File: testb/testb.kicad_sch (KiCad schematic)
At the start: 3 parts

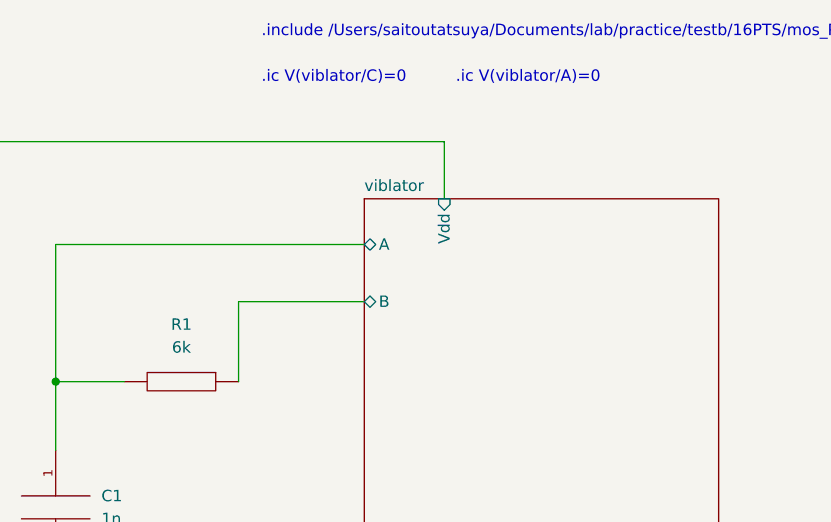
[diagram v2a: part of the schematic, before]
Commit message: マルチフィンガーにせず設計
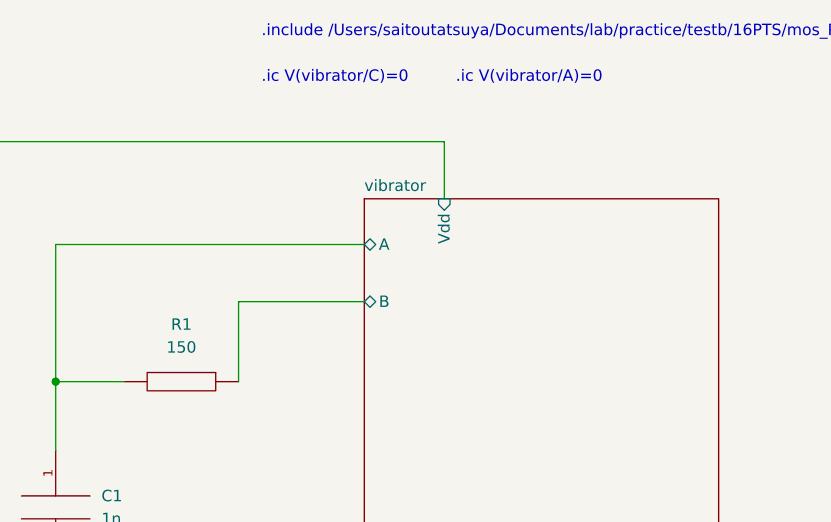
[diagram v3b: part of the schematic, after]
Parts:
- R1: value 6k -> 150
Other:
- sheet viblator renamed vibrator
- note added: ".ic V(vibrator/A)=0"
- note added: ".ic V(vibrator/C)=0"
- note removed: ".ic V(viblator/A)=0"
- note removed: ".ic V(viblator/C)=0"
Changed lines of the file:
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@@
     (stroke (width 0) (type default) (color 0 0 0 0))
   )
-  (text ".ic V(viblator/C)=0" (at 130.81 41.91 0)
+  (text ".ic V(vibrator/C)=0" (at 130.81 41.91 0)
     (effects (font (size 1.27 1.27)) (justify left bottom))
   )
-  (text ".ic V(viblator/A)=0" (at 152.4 41.91 0)
+  (text ".ic V(vibrator/A)=0" (at 152.4 41.91 0)
     (effects (font (size 1.27 1.27)) (justify left bottom))
   )
@@
     (in_bom yes) (on_board yes) (fields_autoplaced)
     (property "Reference" "R1" (id 0) (at 121.92 68.58 90))
-    (property "Value" "6k" (id 1) (at 121.92 71.12 90))
+    (property "Value" "150" (id 1) (at 121.92 71.12 90))
     (property "Footprint" "" (id 2) (at 121.92 74.93 0)
       (effects (font (size 1.27 1.27)) hide)
@@
     (stroke (width 0.1524) (type solid) (color 0 0 0 0))
     (fill (color 0 0 0 0.0000))
-    (property "Sheet name" "viblator" (id 0) (at 142.24 53.8984 0)
+    (property "Sheet name" "vibrator" (id 0) (at 142.24 53.8984 0)
       (effects (font (size 1.27 1.27)) (justify left bottom))
     )
@@
     )
     (path "/2cfb77fc-63f8-4888-94b3-0e86a309ac26"
-      (reference "R1") (unit 1) (value "6k") (footprint "")
+      (reference "R1") (unit 1) (value "150") (footprint "")
     )
     (path "/b717cf87-ea15-43bb-92fa-e84e251c65e1"
